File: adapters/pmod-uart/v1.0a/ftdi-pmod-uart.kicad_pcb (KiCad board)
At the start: 2 copper layers, 16 x 18 mm, 2 parts, among them J1 Conn, J4 Prog

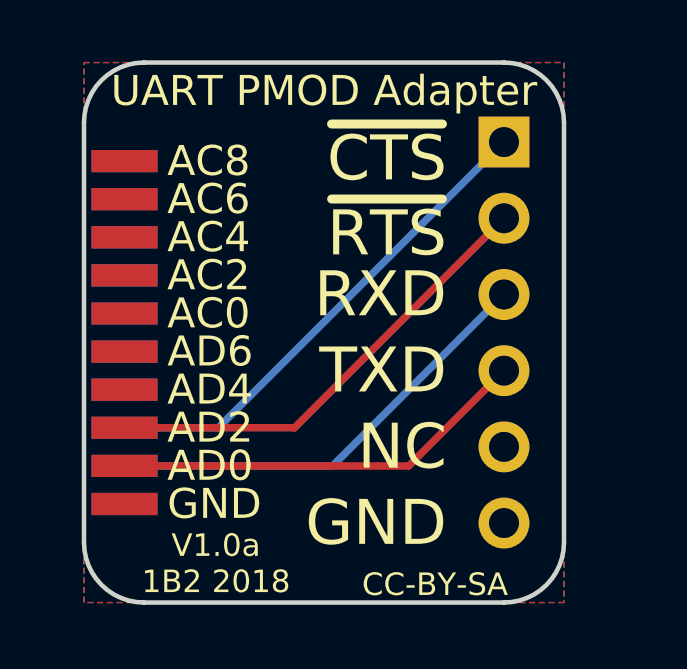
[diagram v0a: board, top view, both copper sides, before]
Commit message: Corrected pmod UART pinout and added INT/RST pins.
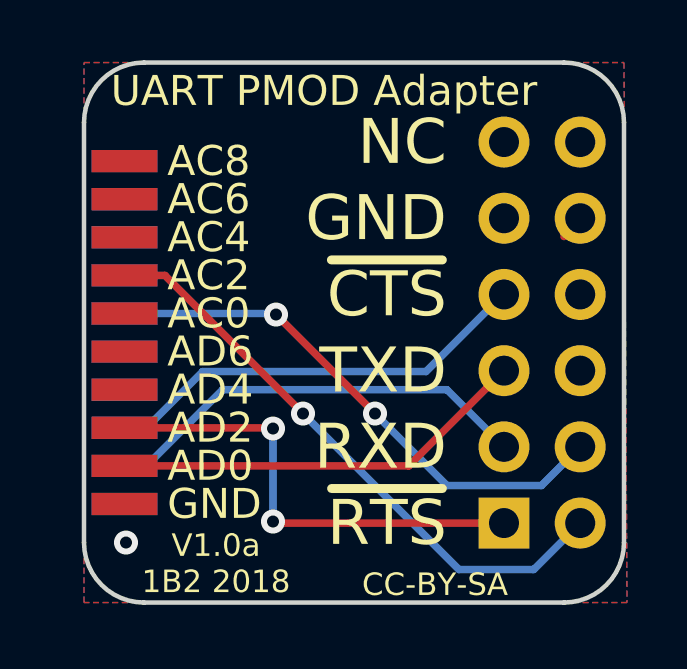
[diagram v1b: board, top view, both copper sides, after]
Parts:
- J4: value Prog -> PMOD; footprint Connector_PinSocket_2.54mm:PinSocket_1x06_P2.54mm_Vertical -> Connector_PinHeader_2.54mm:PinHeader_2x06_P2.54mm_Horizontal
- moved J4 12.7 mm to (44.0, 50.4), turned to 0 degrees
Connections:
- net /~WRSAV renamed /~PWRSAV
- J4 pad 1: /~CTS -> /~RTS
- J4 pad 2: /~RTS -> /ACBUS2
- J4 pad 4: /TXD -> /ACBUS1
- J4 pad 5: Net-(J4-Pad5) -> /TXD
- J4 pad 6: GND -> Net-(J4-Pad6)
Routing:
- net /ACBUS2: track 0.00 -> 19.9 mm, vias 0 -> 1
- net /ACBUS1: track 0.00 -> 18.1 mm, vias 0 -> 2
- net /~CTS: track 16.6 -> 14.5 mm
- net GND: track 0.00 -> 0.61 mm, vias 0 -> 1
- net /RXD: track 15.0 -> 14.5 mm
- net /~RTS: track 15.5 -> 15.8 mm, vias 0 -> 2
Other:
- board size 16 x 18 mm -> 18 x 18 mm

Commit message: A bunch of minor fixes.
* PWRSAV instead of WRSAV in signal table.
* 0.05 solder stop opening instead of 0.2
* Better copper fill parameters.
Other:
- rule pad_to_mask_clearance: 0.2 -> 0.05
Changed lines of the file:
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@@
     (pad_size 1.524 1.524)
     (pad_drill 0.762)
-    (pad_to_mask_clearance 0.2)
+    (pad_to_mask_clearance 0.05)
     (aux_axis_origin 0 0)
     (grid_origin 44 44)
